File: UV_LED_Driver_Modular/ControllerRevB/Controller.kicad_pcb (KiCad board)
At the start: 2 copper layers, 55.2 x 33 mm, 24 parts, among them J1 Barrel_Jack, J2 Conn_01x05, J3 Conn_02x08_Odd_Even, J4 Conn_02x04_Odd_Even, Q1 MMBT3904, SW1 SW_SPST, SW2 Rotary_Encoder, SW3 SW_SPST, SW4 SW_SPST, U1 STM32F051K8Tx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

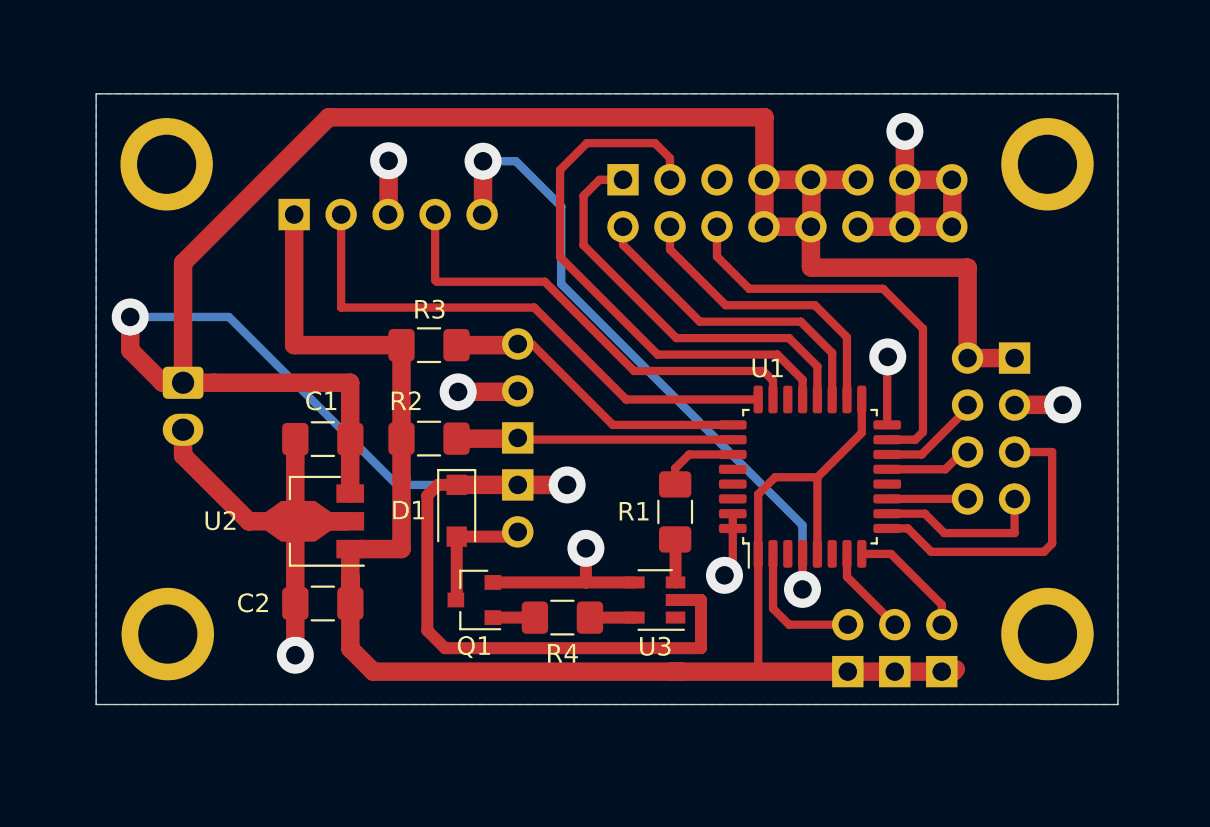
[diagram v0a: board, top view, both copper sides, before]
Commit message: Updated prototype designs for fab
updated readme
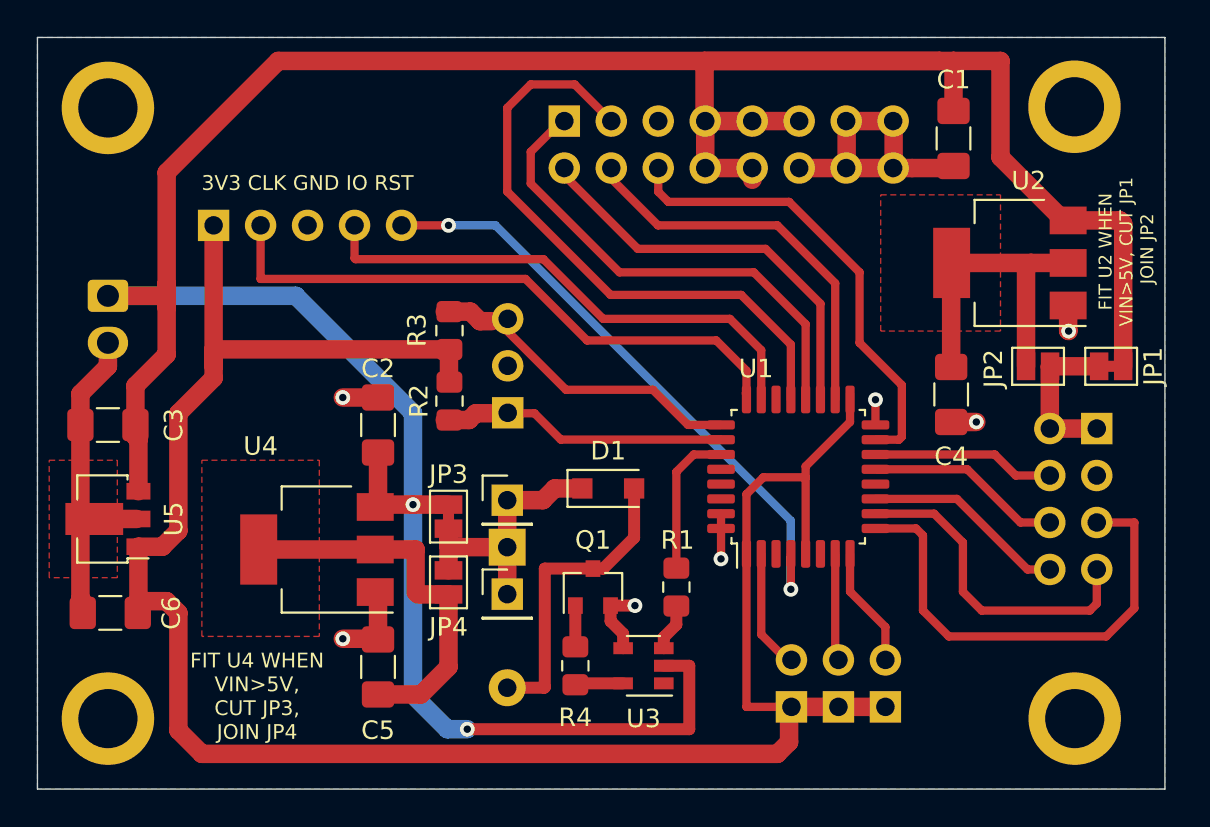
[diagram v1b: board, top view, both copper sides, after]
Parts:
- added C3: 1uF, Capacitor_SMD:C_1206_3216Metric_Pad1.42x1.75mm_HandSolder, F.Cu at (105.4, 109.9)
- added C4: 10uF, Capacitor_SMD:C_1206_3216Metric_Pad1.42x1.75mm_HandSolder, F.Cu at (151.0, 108.2)
- added C5: 10uF, Capacitor_SMD:C_1206_3216Metric_Pad1.42x1.75mm_HandSolder, F.Cu at (120.0, 122.9)
- added C6: 1uF, Capacitor_SMD:C_1206_3216Metric_Pad1.42x1.75mm_HandSolder, F.Cu at (105.5, 120.0)
- added J5: Conn_01x01, Connector_PinHeader_2.54mm:PinHeader_1x01_P2.54mm_Vertical, F.Cu at (127.0, 119.0)
- added J6: Conn_01x01, Connector_PinHeader_2.54mm:PinHeader_1x01_P2.54mm_Vertical, F.Cu at (127.0, 113.9)
- added JP1: Jumper_NC_Small, Jumper:SolderJumper-2_P1.3mm_Bridged_Pad1.0x1.5mm, F.Cu at (159.7, 106.7)
- added JP2: Jumper_NO_Small, Jumper:SolderJumper-2_P1.3mm_Open_Pad1.0x1.5mm, F.Cu at (155.7, 106.7)
- added JP3: Jumper_NC_Small, Jumper:SolderJumper-2_P1.3mm_Bridged_Pad1.0x1.5mm, F.Cu at (123.8, 114.8)
- added JP4: Jumper_NO_Small, Jumper:SolderJumper-2_P1.3mm_Open_Pad1.0x1.5mm, F.Cu at (123.8, 118.4)
- added U4: LD1117S50TR_SOT223, Package_TO_SOT_SMD:SOT-223-3_TabPin2, F.Cu at (116.7, 116.6)
- added U5: L78L33_SOT89, Package_TO_SOT_SMD:SOT-89-3, F.Cu at (105.4, 114.9)
- BZ1: footprint Connector_PinHeader_2.54mm:PinHeader_1x02_P2.54mm_Vertical -> Buzzer_Beeper:Buzzer_12x9.5RM7.6
- C1, C2: value 1uF -> 100nF
- R1, R2, R3, R4: footprint Resistor_SMD:R_1206_3216Metric_Pad1.42x1.75mm_HandSolder -> Resistor_SMD:R_0805_2012Metric_Pad1.15x1.40mm_HandSolder
- U2: value L78L33_SOT89 -> LD1117S50TR_SOT223; footprint Package_TO_SOT_SMD:SOT-89-3 -> Package_TO_SOT_SMD:SOT-223-3_TabPin2
- moved U2 39.7 mm to (154.2, 101.1)
- moved C1 37.8 mm to (151.1, 94.4), turned to 270 degrees
- moved C2 10.1 mm to (120.0, 109.9), turned to 90 degrees
- moved D1 8.28 mm to (132.5, 113.3), turned to 0 degrees
- moved Q1 6.45 mm to (131.6, 118.6), turned to 90 degrees
- moved J1 6.21 mm to (105.4, 102.9)
- moved J4 5.85 mm to (158.9, 110.0)
- moved REF** 5.60 mm to (105.4, 125.7)
- moved REF** 4.80 mm to (157.7, 125.7)
- moved J3 4.49 mm to (130.1, 93.4)
- moved REF** 4.40 mm to (105.4, 92.7)
- moved J2 4.40 mm to (111.1, 99.1)
- moved R1 4.06 mm to (136.1, 118.6)
- moved U3 3.61 mm to (134.4, 122.9)
- moved SW1 3.59 mm to (142.4, 125.1)
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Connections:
- BZ1 pad 1: VPP -> Net-(BZ1-Pad1)
- C2 pad 1: +3V3 -> VPP
- D1 pad 1: VPP -> Net-(BZ1-Pad1)
- J4 pad 1: VPP -> /LED_Controller_Module/TFT_LED
- J4 pad 2: VPP -> /LED_Controller_Module/TFT_LED
- U2 pad 1: +3V3 -> GNDS
- U2 pad 2: GNDS -> /LED_Controller_Module/LCD_5V
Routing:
- net +3V3: track 88.8 -> 115.0 mm
- net VPP: track 157.4 -> 180.9 mm
- net /LED_Controller_Module/PIEZO_5V: track 0.00 -> 20.9 mm
- net GNDS: track 68.7 -> 50.8 mm, vias 8 -> 7
- net /LED_Controller_Module/LCD_5V: track 0.00 -> 17.6 mm
- net Net-(BZ1-Pad1): track 0.00 -> 15.5 mm
- net Net-(BZ1-Pad2): track 6.84 -> 16.6 mm
- net /LED_Controller_Module/TFT_CS: track 16.6 -> 26.1 mm
- net /LED_Controller_Module/TFT_LED: track 0.00 -> 8.56 mm
- net /LED_Controller_Module/TFT_DC: track 9.49 -> 18.0 mm
- net /LED_Controller_Module/TFT_SCK: track 4.35 -> 11.0 mm
- net /LED_Controller_Module/TFT_MOSI: track 4.84 -> 10.6 mm
- net /LED_PWM_OUT4: track 16.1 -> 21.3 mm
- net /LED_PWM_OUT3: track 17.2 -> 22.3 mm
- net /LED_Controller_Module/TFT_RST: track 5.83 -> 9.90 mm
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- added copper zone on F.Cu, net /LED_Controller_Module/LCD_5V
- added copper zone on F.Cu, net /LED_Controller_Module/PIEZO_5V
- added copper zone on F.Cu, net GNDS
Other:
- board size 55.2 x 33 mm -> 61 x 40.6 mm
- board text added: "+"
- board text added: "-"
- board text added: "2 1 VPP GND"
- board text added: "3 4 5 VPP GND"
- board text added: "3V3 CLK GND IO RST"
- board text added: "< 3V3"
- board text added: "DISPLAY"
- board text added: "ENCODER"
- board text added: "FIT U2 WHEN VIN>5V, CUT JP1 JOIN JP2"
- board text added: "FIT U4 WHEN VIN>5V, CUT JP3, JOIN JP4"
- board text added: "LCD CONTROLLER 0620 RevB"
- board text added: "MAX 5V WITHOUT U2 + U4"
- board text added: "PWR"
- board text added: "RST IO GND CLK 3V3"
- board text added: "SIGNAL/POWER BUS"
- board text added: "SWITCHES"

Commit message: added pull down resistor to MCU to prevent buzzer from sounding at boot
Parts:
- R1: value 1K -> 10K
- moved R1 0.75 mm to (136.4, 117.9), turned to 180 degrees
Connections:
- R1 pad 1: Net-(R1-Pad1) -> GNDS
- U3 pad 3: Net-(R1-Pad1) -> /LED_Controller_Module/BUZZER_PWM
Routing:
- net /LED_Controller_Module/BUZZER_PWM: track 8.01 -> 13.0 mm
- net GNDS: track 50.8 -> 54.2 mm
- net Net-(R1-Pad1): track 2.56 -> 0.00 mm
